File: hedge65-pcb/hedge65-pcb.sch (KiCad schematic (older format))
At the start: 164 parts, among them J1 USB_C_Receptacle_USB2.0, SW1 SW_PUSH, U1 ATmega32U4-AU, Y1 16MHz

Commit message: schematic done
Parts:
- C1, C2, C3, C4, C5, C6, C7: footprint (none) -> Capacitor_SMD:C_0805_2012Metric
- D1, D10, D11, D12, D13, D14, D15, D16, D17, D18, D19, D2, D20, D21, D22, D23, D24, D25, D26, D27, D28, D29, D3, D30, D31, D32, D33, D34, D35, D36, D37, D38, D39, D4, D40, D41, D42, D43, D44, D45, D46, D47, D48, D49, D5, D50, D51, D52, D53, D54, D55, D56, D57, D58, D59, D6, D60, D61, D62, D63, D64, D65, D66, D67, D68, D69, D7, D70, D71, D72, D73, D8, D9: footprint (none) -> Diode_SMD:D_SOD-123
- F1: footprint (none) -> Fuse:Fuse_1206_3216Metric
- J1: footprint (none) -> Type-C:HRO-TYPE-C-31-M-12-HandSoldering
- Y1: footprint (none) -> Crystal:Crystal_SMD_3225-4Pin_3.2x2.5mm

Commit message: redo
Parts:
- removed F1: 500mA, Fuse:Fuse_1206_3216Metric, symbol Device:Polyfuse
- removed J1: USB_C_Receptacle_USB2.0, Type-C:HRO-TYPE-C-31-M-12-HandSoldering, symbol Connector:USB_C_Receptacle_USB2.0
- removed R5, R6: 5.1k, Resistor_SMD:R_0805_2012Metric, symbol Device:R_Small
- removed U1: ATmega32U4-AU, Package_QFP:TQFP-44_10x10mm_P0.8mm, symbol MCU_Microchip_ATmega:ATmega32U4-AU
- removed Y1: 16MHz, Crystal:Crystal_SMD_3225-4Pin_3.2x2.5mm, symbol Device:Crystal_GND24_Small
- added J1: USB_C_Receptacle, symbol Connector:USB_C_Receptacle
- added U1: ATMEGA32U4, ATmega32U4:ATmega32U4, symbol keyboard_parts:ATMEGA32U4
- added X1: XTAL_GND, Crystal:Crystal_SMD_3225-4Pin_3.2x2.5mm, symbol keyboard_parts:XTAL_GND
- C1: value 0.1uF -> 22p
- C2: value 22pF -> 22p
- C3: value 22pF -> 0.1u
- C4, C5: value 0.1uF -> 0.1u
- C6: value 1uF -> 0.1u
- C7: value 10uF -> 4.7u
- D1, D10, D11, D12, D13, D14, D15, D16, D17, D18, D19, D2, D20, D21, D22, D23, D24, D25, D26, D27, D28, D29, D3, D30, D31, D32, D33, D34, D35, D36, D37, D38, D39, D4, D40, D41, D42, D43, D44, D45, D46, D47, D48, D49, D5, D50, D51, D52, D53, D54, D55, D56, D57, D58, D59, D6, D60, D61, D62, D63, D64, D65, D66, D67, D68, D69, D7, D70, D71, D72, D73, D8, D9: footprint Diode_SMD:D_SOD-123 -> cftkb:D_DO-35_SOD27_P5.08mm_Horizontal
- R1, R2: value 22 -> R_Small
- R3, R4: value 10k -> R_Small
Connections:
- net D+ is gone; now on net +5V: R2.1
- net D- is gone; now on net +5V: R1.1
- net +5V: now also C2.2, R4.1, J1.A1 (GND), J1.A12 (GND), J1.B1 (GND), J1.B12 (GND), U1.15 (GND), U1.23 (GND), U1.35 (GND), U1.43 (GND), U1.5 (UGnd), X1.3; no longer C1.1, C2.1, C3.1, C4.1, C4.2, C5.1, C5.2, C6.2, C7.1, C7.2, R3.1, R4.2
- net VCC: now also C3.1, C4.1, C5.1, C6.1, C7.1, R3.2, J1.A4 (VBUS), J1.A9 (VBUS), J1.B4 (VBUS), J1.B9 (VBUS), U1.14 (VCC), U1.2 (UVcc), U1.24 (AVCC), U1.34 (VCC), U1.44 (AVCC)
- net col1: now also U1.36 (PF7)
- net col10: now also U1.8 (PB0/SS)
- net col11: now also U1.9 (PB1/SCK)
- net col12: now also U1.10 (PB2/MOSI)
- net col13: now also U1.11 (PB3/MISO)
- net col14: now also U1.12 (PB7/~RTS)
- net col15: now also U1.18 (PD0/INT0)
- net col2: now also U1.32 (PC7)
- net col3: now also U1.31 (PC6)
- net col4: now also U1.30 (PB6)
- net col5: now also U1.29 (PB5)
- net col6: now also U1.28 (PB4)
- net col7: now also U1.27 (T0/PD7)
- net col8: now also U1.26 (T1/PD6)
- net col9: now also U1.25 (ICP1/PD4)
- net row0: now also U1.41 (PF0)
- net row1: now also U1.40 (PF1)
- net row2: now also U1.39 (PF4)
- net row3: now also U1.38 (PF5)
- net row4: now also U1.37 (PF6)
- net at SW1.2: now also R3.1, U1.13 (~RESET); no longer R3.2
- net at C3.2: now also C4.2, C5.2, C6.2, C7.2
- net at R1.2: now also J1.A5 (CC1)
- net at R2.2: now also J1.B5 (CC2)
- new net: C1.1, U1.16 (XTAL1), X1.1
- new net: C2.1, U1.17 (XTAL2), X1.2
- new net: J1.A7 (D-), J1.B7 (D-), U1.3 (D-)
- new net: R4.2, U1.33 (~HWB/PE2)
- new net: J1.A6 (D+), J1.B6 (D+), U1.4 (D+)
- no-connect marks 2 -> 14

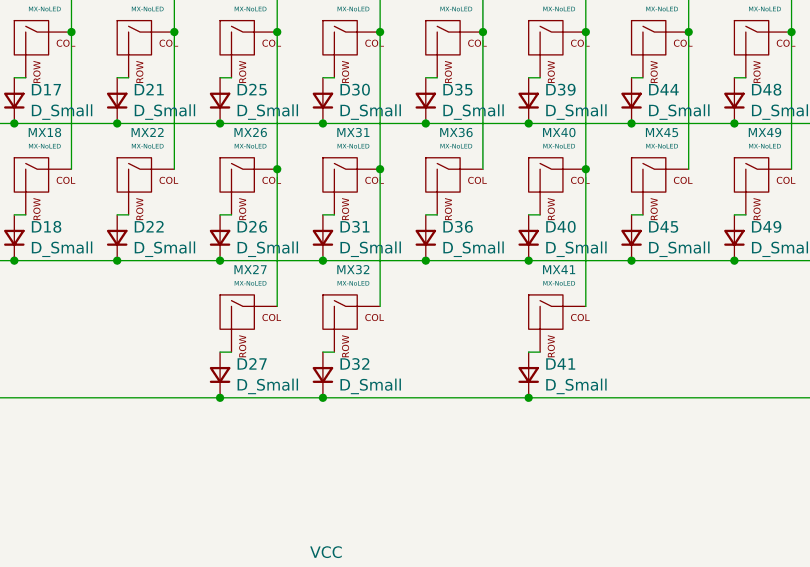
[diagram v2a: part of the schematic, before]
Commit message: doides shifted to deadspace
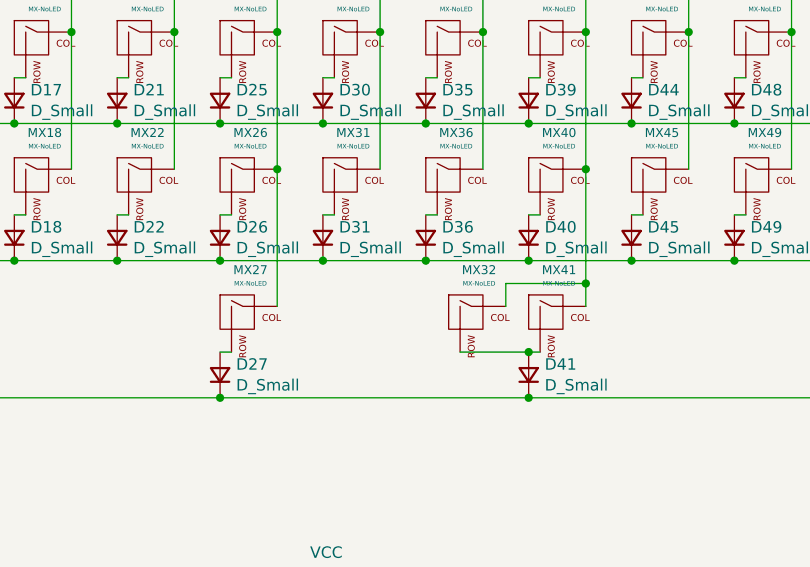
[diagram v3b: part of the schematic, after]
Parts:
- removed D32: D_Small, cftkb:D_DO-35_SOD27_P5.08mm_Horizontal, symbol Device:D_Small
- J1: footprint (none) -> Connector_USB:USB_C_Receptacle_Amphenol_12401548E4-2A_CircularHoles
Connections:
- net col6: no longer MX32.1 (COL)
- net col8: now also MX32.1 (COL)
- net at MX32.2 (ROW): now also D41.2 (A), MX41.2 (ROW)
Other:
- moved on the sheet: MX32
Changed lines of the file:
@@
 Connection ~ 3600 1900
 Connection ~ 4050 1900
-Connection ~ 3600 2500
 $Comp
 L MX_Alps_Hybrid:MX-NoLED MX32
 U 1 1 6000346A
-P 3450 3150
-F 0 "MX32" H 3483 3359 39  0000 C CNN
-F 1 "MX-NoLED" H 3483 3300 20  0000 C CNN
-F 2 "MX_Alps_Hybrid:MX-1U-NoLED" H 2825 3125 60  0001 C CNN
-F 3 "" H 2825 3125 60  0001 C CNN
-	1    3450 3150
-	1    0    0    -1
-$EndComp
-$Comp
-L Device:D_Small D32
-U 1 1 60003470
-P 3350 3400
-F 0 "D32" V 3396 3330 50  0000 R CNN
-F 1 "D_Small" V 3305 3330 50  0000 R CNN
-F 2 "cftkb:D_DO-35_SOD27_P5.08mm_Horizontal" V 3350 3400 50  0001 C CNN
-F 3 "~" V 3350 3400 50  0001 C CNN
-	1    3350 3400
-	0    -1   -1   0
-$EndComp
-Wire Wire Line
-	3350 3300 3400 3300
-Wire Wire Line
-	3600 2500 3600 3100
-Connection ~ 3350 3500
+P 4000 3150
+F 0 "MX32" H 4033 3359 39  0000 C CNN
+F 1 "MX-NoLED" H 4033 3300 20  0000 C CNN
+F 2 "MX_Alps_Hybrid:MX-1U-NoLED" H 3375 3125 60  0001 C CNN
+F 3 "" H 3375 3125 60  0001 C CNN
+	1    4000 3150
+	1    0    0    -1
+$EndComp
 Wire Wire Line
 	2900 1100 3350 1100
@@
 	2900 2900 3350 2900
 Connection ~ 2900 2900
-Wire Wire Line
-	2900 3500 3350 3500
 Connection ~ 2900 3500
 $Comp
@@
 	4250 3300 4300 3300
 Wire Wire Line
-	4500 2500 4500 3100
+	4500 2500 4500 3000
 Connection ~ 4250 3500
 Wire Wire Line
@@
 Wire Wire Line
 	1550 3500 2900 3500
-Wire Wire Line
-	3350 3500 4250 3500
 Wire Wire Line
 	4250 3500 5600 3500
@@
 F 0 "J1" H 1407 7067 50  0000 C CNN
 F 1 "USB_C_Receptacle" H 1407 6976 50  0000 C CNN
-F 2 "" H 1450 5800 50  0001 C CNN
+F 2 "Connector_USB:USB_C_Receptacle_Amphenol_12401548E4-2A_CircularHoles" H 1450 5800 50  0001 C CNN
 F 3 "https://www.usb.org/sites/default/files/documents/usb_type-c.zip" H 1450 5800 50  0001 C CNN
 	1    1300 5800
@@
 	4650 4800 4350 4800
 Connection ~ 4350 4800
+Wire Wire Line
+	2900 3500 4250 3500
+Wire Wire Line
+	3950 3300 4250 3300
+Connection ~ 4250 3300
+Wire Wire Line
+	4150 3100 4150 3000
+Wire Wire Line
+	4150 3000 4500 3000
+Connection ~ 4500 3000
+Wire Wire Line
+	4500 3000 4500 3100
 $EndSCHEMATC
